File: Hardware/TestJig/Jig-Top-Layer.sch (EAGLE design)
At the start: 3 parts

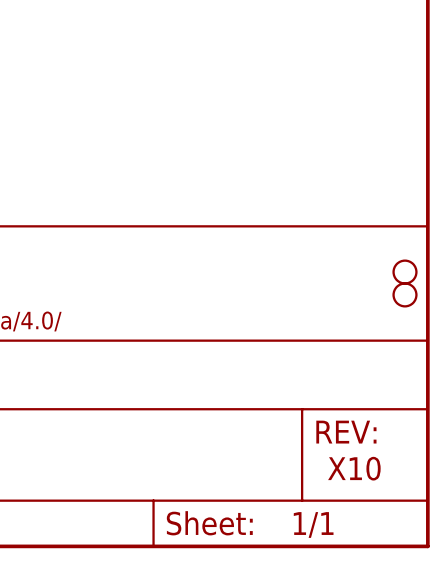
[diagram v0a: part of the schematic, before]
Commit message: Tweaked testjig middle and top layers
middle layer changes:
-changed holes for the pogopins to pup up through from pads to actual "holes" in eagle file. removed pads from sch and board.
-set hole size to 0.055 inch diameter for optimal lazer cutting in acrylic.

top layer changes:
-tightened up frame to huge product dimensions with 0.016 inch gap.
-added corner cutouts
-added "lift-out" cutout on the side, for easier product removal

Also note, bumped outer dimensions on both middle and top to allow for more strength around the corner standoff holes. Previous deisgn would probably crack if cut in acrylic with lazer.
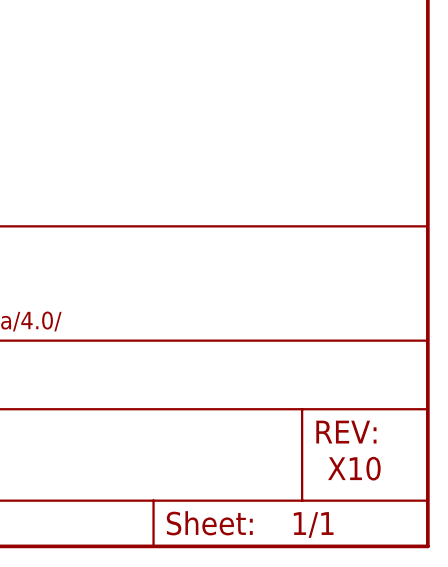
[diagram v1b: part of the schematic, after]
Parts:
- removed JP3, JP4: STAND-OFF, SparkFun:STAND-OFF
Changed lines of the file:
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@@
 <?xml version="1.0" encoding="utf-8"?>
 <!DOCTYPE eagle SYSTEM "eagle.dtd">
-<eagle version="7.7.0">
+<eagle version="7.6.0">
 <drawing>
 <settings>
@@
 </classes>
 <parts>
-<part name="JP3" library="SparkFun" deviceset="STAND-OFF" device=""/>
-<part name="JP4" library="SparkFun" deviceset="STAND-OFF" device=""/>
 <part name="FRAME1" library="SparkFun-Aesthetics" deviceset="FRAME-LETTER" device=""/>
 </parts>
@@
 </plain>
 <instances>
-<instance part="JP3" gate="G$1" x="246.38" y="30.48"/>
-<instance part="JP4" gate="G$1" x="246.38" y="27.94"/>
 <instance part="FRAME1" gate="G$1" x="0" y="0"/>
 <instance part="FRAME1" gate="V" x="147.32" y="0"/>
